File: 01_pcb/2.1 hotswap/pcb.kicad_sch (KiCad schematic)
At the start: 138 parts, among them J1 TYPE-C-31-M12_13, J2 AVR-ISP-6_mod, J3 Conn_01x01, J4 Conn_01x01, J5 Conn_01x01, J6 Conn_01x01, J7 Conn_01x01, J8 4PIN, K1 KEYSW, K10 KEYSW, K11 KEYSW, K12 KEYSW, K13 KEYSW, K14 KEYSW, K15 KEYSW, K16 KEYSW, K17 KEYSW, K18 KEYSW, K19 KEYSW, K2 KEYSW, K20 KEYSW, K21 KEYSW, K22 KEYSW, K23 KEYSW, K24 KEYSW, K25 KEYSW, K26 KEYSW, K27 KEYSW, K28 KEYSW, K29 KEYSW, K3 KEYSW, K30 KEYSW, K31 KEYSW, K32 KEYSW, K33 KEYSW, K34 KEYSW, K35 KEYSW, K36 KEYSW, K37 KEYSW, K38 KEYSW, K39 KEYSW, K4 KEYSW, K40 KEYSW, K41 KEYSW, K42 KEYSW, K43 KEYSW, K44 KEYSW, K45 KEYSW, K46 KEYSW, K47 KEYSW, K48 KEYSW, K49 KEYSW, K5 KEYSW, K50 KEYSW, K51 KEYSW, K52 KEYSW, K6 KEYSW, K7 KEYSW, K8 KEYSW, K9 KEYSW, SW1 SW_PUSH, SW2 Rotary_Encoder_Switch, U1 ATMEGA32U4, U2 PRTR5V0U2X, Y1 16MHz

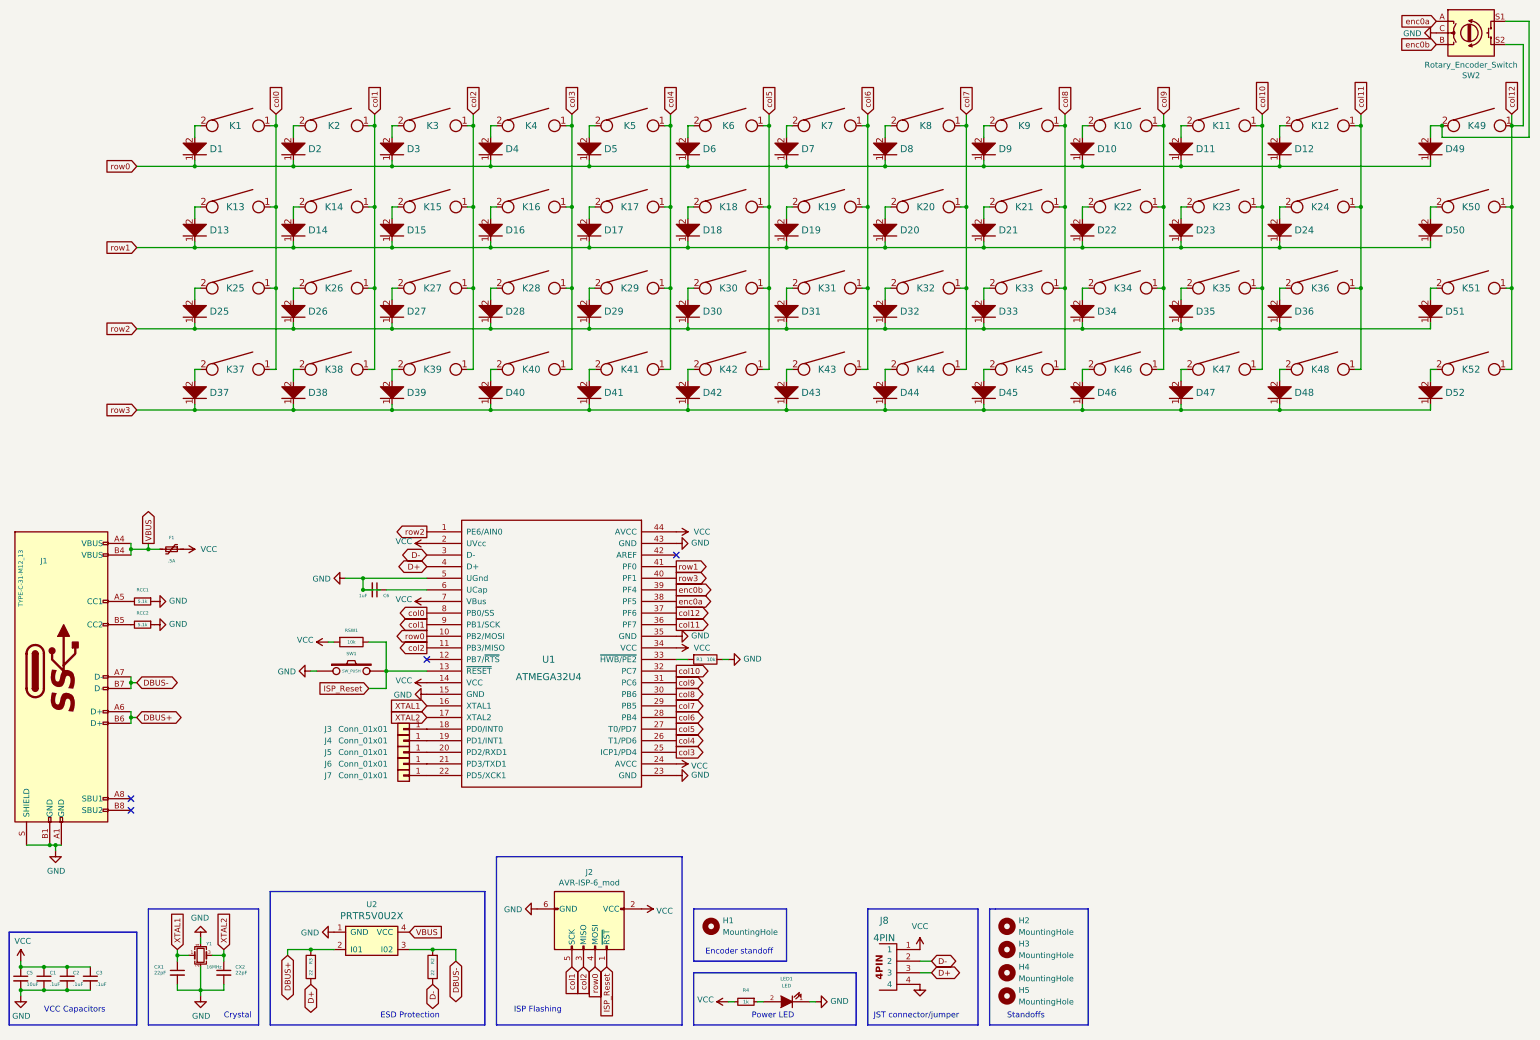
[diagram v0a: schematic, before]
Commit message: remove flex cuts and encoder
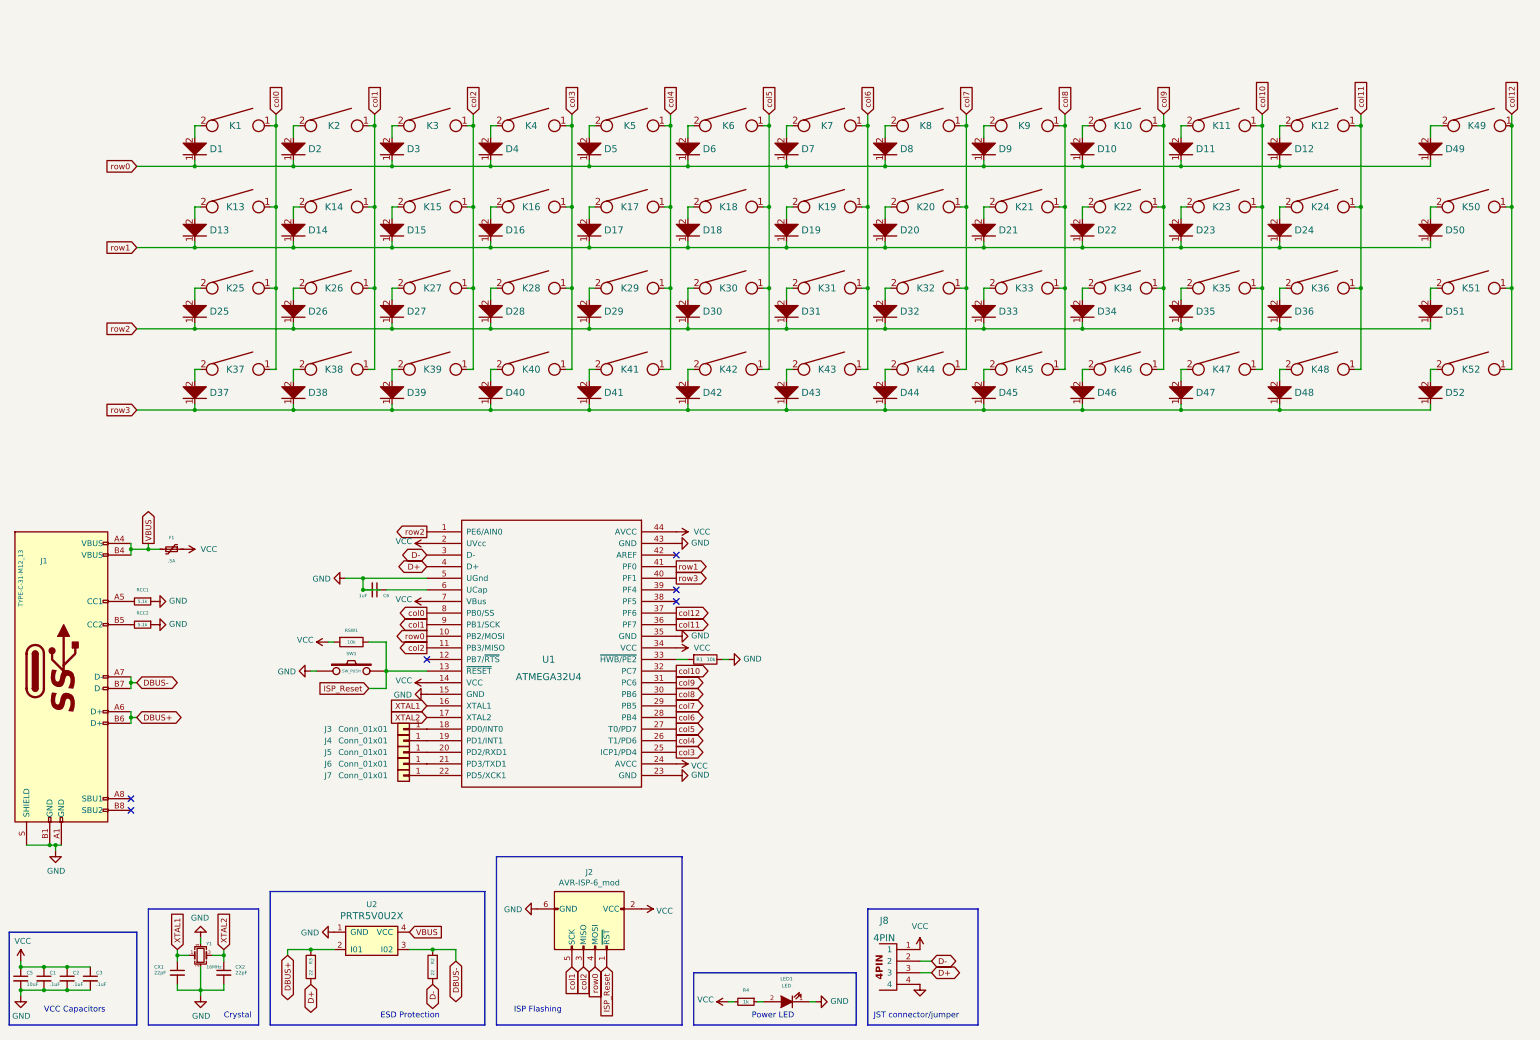
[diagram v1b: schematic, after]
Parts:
- removed H1, H2, H3, H4, H5: MountingHole, MountingHole:MountingHole_2.2mm_M2_DIN965_Pad, symbol Mechanical:MountingHole
- removed SW2: Rotary_Encoder_Switch, Keebio-Parts:RotaryEncoder_EC11, symbol Device:Rotary_Encoder_Switch
- K49: footprint MX_Only:MXOnly-1U-NoLED -> MX_Only:MXOnly-1U-Hotswap
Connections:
- net enc0a: no longer names the net of U1.38 (PF5)
- net enc0b: no longer names the net of U1.39 (PF4)
- no-connect marks 4 -> 6
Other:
- note removed: "Encoder standoff"
- note removed: "Standoffs"

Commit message: add 3d models to kicad footprints
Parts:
- R1, R2, R3, R4, RCC1, RCC2, RSW1: footprint Resistor_SMD:R_0805_2012Metric_Pad1.15x1.40mm_HandSolder -> Keeb_footprints:R_0805_2012Metric_Pad1.20x1.40mm_HandSolder
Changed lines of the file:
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@@
       (effects (font (size 0.7112 0.7112)))
     )
-    (property "Footprint" "Resistor_SMD:R_0805_2012Metric_Pad1.15x1.40mm_HandSolder" (id 2) (at 72.39 154.94 0)
+    (property "Footprint" "Keeb_footprints:R_0805_2012Metric_Pad1.20x1.40mm_HandSolder" (id 2) (at 72.39 154.94 0)
       (effects (font (size 1.27 1.27)) hide)
     )
@@
       (effects (font (size 0.7112 0.7112)))
     )
-    (property "Footprint" "Resistor_SMD:R_0805_2012Metric_Pad1.15x1.40mm_HandSolder" (id 2) (at 72.39 149.86 0)
+    (property "Footprint" "Keeb_footprints:R_0805_2012Metric_Pad1.20x1.40mm_HandSolder" (id 2) (at 72.39 149.86 0)
       (effects (font (size 1.27 1.27)) hide)
     )
@@
       (effects (font (size 0.7112 0.7112)))
     )
-    (property "Footprint" "Resistor_SMD:R_0805_2012Metric_Pad1.15x1.40mm_HandSolder" (id 2) (at 118.11 156.972 90)
+    (property "Footprint" "Keeb_footprints:R_0805_2012Metric_Pad1.20x1.40mm_HandSolder" (id 2) (at 118.11 156.972 90)
       (effects (font (size 1.27 1.27)) hide)
     )
@@
       (effects (font (size 0.762 0.762)))
     )
-    (property "Footprint" "Resistor_SMD:R_0805_2012Metric_Pad1.15x1.40mm_HandSolder" (id 2) (at 195.58 160.782 90)
+    (property "Footprint" "Keeb_footprints:R_0805_2012Metric_Pad1.20x1.40mm_HandSolder" (id 2) (at 195.58 160.782 90)
       (effects (font (size 1.27 1.27)) hide)
     )
@@
       (effects (font (size 0.7112 0.7112)))
     )
-    (property "Footprint" "Resistor_SMD:R_0805_2012Metric_Pad1.15x1.40mm_HandSolder" (id 2) (at 137.668 229.87 90)
+    (property "Footprint" "Keeb_footprints:R_0805_2012Metric_Pad1.20x1.40mm_HandSolder" (id 2) (at 137.668 229.87 90)
       (effects (font (size 1.27 1.27)) hide)
     )
@@
       (effects (font (size 0.7112 0.7112)))
     )
-    (property "Footprint" "Resistor_SMD:R_0805_2012Metric_Pad1.15x1.40mm_HandSolder" (id 2) (at 110.998 229.87 90)
+    (property "Footprint" "Keeb_footprints:R_0805_2012Metric_Pad1.20x1.40mm_HandSolder" (id 2) (at 110.998 229.87 90)
       (effects (font (size 1.27 1.27)) hide)
     )
@@
       (effects (font (size 0.762 0.762)))
     )
-    (property "Footprint" "Resistor_SMD:R_0805_2012Metric_Pad1.15x1.40mm_HandSolder" (id 2) (at 204.47 237.49 0)
+    (property "Footprint" "Keeb_footprints:R_0805_2012Metric_Pad1.20x1.40mm_HandSolder" (id 2) (at 204.47 237.49 0)
       (effects (font (size 1.27 1.27)) hide)
     )
@@
     )
     (path "/00000000-0000-0000-0000-00005e28a0b7"
-      (reference "R1") (unit 1) (value "10k") (footprint "Resistor_SMD:R_0805_2012Metric_Pad1.15x1.40mm_HandSolder")
+      (reference "R1") (unit 1) (value "10k") (footprint "Keeb_footprints:R_0805_2012Metric_Pad1.20x1.40mm_HandSolder")
     )
     (path "/00000000-0000-0000-0000-00005e4290ae"
-      (reference "R2") (unit 1) (value "22") (footprint "Resistor_SMD:R_0805_2012Metric_Pad1.15x1.40mm_HandSolder")
+      (reference "R2") (unit 1) (value "22") (footprint "Keeb_footprints:R_0805_2012Metric_Pad1.20x1.40mm_HandSolder")
     )
     (path "/00000000-0000-0000-0000-00005e44c75b"
-      (reference "R3") (unit 1) (value "22") (footprint "Resistor_SMD:R_0805_2012Metric_Pad1.15x1.40mm_HandSolder")
+      (reference "R3") (unit 1) (value "22") (footprint "Keeb_footprints:R_0805_2012Metric_Pad1.20x1.40mm_HandSolder")
     )
     (path "/00000000-0000-0000-0000-00005f9dc91d"
-      (reference "R4") (unit 1) (value "1k") (footprint "Resistor_SMD:R_0805_2012Metric_Pad1.15x1.40mm_HandSolder")
+      (reference "R4") (unit 1) (value "1k") (footprint "Keeb_footprints:R_0805_2012Metric_Pad1.20x1.40mm_HandSolder")
     )
     (path "/00000000-0000-0000-0000-00005dd97927"
-      (reference "RCC1") (unit 1) (value "5.1k") (footprint "Resistor_SMD:R_0805_2012Metric_Pad1.15x1.40mm_HandSolder")
+      (reference "RCC1") (unit 1) (value "5.1k") (footprint "Keeb_footprints:R_0805_2012Metric_Pad1.20x1.40mm_HandSolder")
     )
     (path "/00000000-0000-0000-0000-00005dd95fdc"
-      (reference "RCC2") (unit 1) (value "5.1k") (footprint "Resistor_SMD:R_0805_2012Metric_Pad1.15x1.40mm_HandSolder")
+      (reference "RCC2") (unit 1) (value "5.1k") (footprint "Keeb_footprints:R_0805_2012Metric_Pad1.20x1.40mm_HandSolder")
     )
     (path "/00000000-0000-0000-0000-00005e1f1159"
-      (reference "RSW1") (unit 1) (value "10k") (footprint "Resistor_SMD:R_0805_2012Metric_Pad1.15x1.40mm_HandSolder")
+      (reference "RSW1") (unit 1) (value "10k") (footprint "Keeb_footprints:R_0805_2012Metric_Pad1.20x1.40mm_HandSolder")
     )
     (path "/00000000-0000-0000-0000-00005e1efd9f"

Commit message: ¯\_(ツ)_/¯
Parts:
- removed J3, J4, J5, J6, J7: Conn_01x01, TestPoint:TestPoint_Keystone_5000-5004_Miniature, symbol Connector_Generic:Conn_01x01
- added J3: Conn_01x05_Female, Connector_PinHeader_2.54mm:PinHeader_1x05_P2.54mm_Vertical, symbol Connector:Conn_01x05_Female
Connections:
- net at U1.18 (PD0/INT0): now also J3.5 (Pin_5)
- net at U1.19 (PD1/INT1): now also J3.4 (Pin_4)
- net at U1.20 (PD2/RXD1): now also J3.3 (Pin_3)
- net at U1.21 (PD3/TXD1): now also J3.2 (Pin_2)
- net at U1.22 (PD5/XCK1): now also J3.1 (Pin_1)
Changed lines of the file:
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@@
     (pin "4")
   )
-  (symbol (lib_id "Connector_Generic:Conn_01x01") (at 129.54 177.8 180) (unit 1)
+  (symbol (lib_id "Connector:Conn_01x05_Female") (at 129.54 182.88 180) (unit 1)
     (in_bom yes) (on_board yes)
-    (property "Reference" "J3" (id 0) (at 113.03 177.8 0))
-    (property "Value" "Conn_01x01" (id 1) (at 120.65 177.8 0))
-    (property "Footprint" "TestPoint:TestPoint_Keystone_5000-5004_Miniature" (id 2) (at 129.54 177.8 0)
-      (effects (font (size 1.27 1.27)) hide)
-    )
-    (property "Datasheet" "~" (id 3) (at 129.54 177.8 0)
-      (effects (font (size 1.27 1.27)) hide)
-    )
-    (pin "1")
-  )
-  (symbol (lib_id "Connector_Generic:Conn_01x01") (at 129.54 187.96 180) (unit 1)
-    (in_bom yes) (on_board yes)
-    (property "Reference" "J7" (id 0) (at 113.03 187.96 0))
-    (property "Value" "Conn_01x01" (id 1) (at 120.65 187.96 0))
-    (property "Footprint" "TestPoint:TestPoint_Keystone_5000-5004_Miniature" (id 2) (at 129.54 187.96 0)
-      (effects (font (size 1.27 1.27)) hide)
-    )
-    (property "Datasheet" "~" (id 3) (at 129.54 187.96 0)
-      (effects (font (size 1.27 1.27)) hide)
-    )
-    (pin "1")
+    (property "Reference" "J3" (id 0) (at 130.175 172.72 0))
+    (property "Value" "Conn_01x05_Female" (id 1) (at 123.19 182.88 90))
+    (property "Footprint" "Connector_PinHeader_2.54mm:PinHeader_1x05_P2.54mm_Vertical" (id 2) (at 129.54 182.88 0)
+      (effects (font (size 1.27 1.27)) hide)
+    )
+    (property "Datasheet" "~" (id 3) (at 129.54 182.88 0)
+      (effects (font (size 1.27 1.27)) hide)
+    )
+    (pin "1")
+    (pin "2")
+    (pin "3")
+    (pin "4")
+    (pin "5")
   )
   (symbol (lib_id "power:VCC") (at 242.57 226.06 0) (unit 1)
@@
     )
     (property "Datasheet" "" (id 3) (at 242.57 226.06 0)
-      (effects (font (size 1.27 1.27)) hide)
-    )
-    (pin "1")
-  )
-  (symbol (lib_id "Connector_Generic:Conn_01x01") (at 129.54 182.88 180) (unit 1)
-    (in_bom yes) (on_board yes)
-    (property "Reference" "J5" (id 0) (at 113.03 182.88 0))
-    (property "Value" "Conn_01x01" (id 1) (at 120.65 182.88 0))
-    (property "Footprint" "TestPoint:TestPoint_Keystone_5000-5004_Miniature" (id 2) (at 129.54 182.88 0)
-      (effects (font (size 1.27 1.27)) hide)
-    )
-    (property "Datasheet" "~" (id 3) (at 129.54 182.88 0)
       (effects (font (size 1.27 1.27)) hide)
     )
@@
     (pin "4")
   )
-  (symbol (lib_id "Connector_Generic:Conn_01x01") (at 129.54 185.42 180) (unit 1)
-    (in_bom yes) (on_board yes)
-    (property "Reference" "J6" (id 0) (at 113.03 185.42 0))
-    (property "Value" "Conn_01x01" (id 1) (at 120.65 185.42 0))
-    (property "Footprint" "TestPoint:TestPoint_Keystone_5000-5004_Miniature" (id 2) (at 129.54 185.42 0)
-      (effects (font (size 1.27 1.27)) hide)
-    )
-    (property "Datasheet" "~" (id 3) (at 129.54 185.42 0)
-      (effects (font (size 1.27 1.27)) hide)
-    )
-    (pin "1")
-  )
-  (symbol (lib_id "Connector_Generic:Conn_01x01") (at 129.54 180.34 180) (unit 1)
-    (in_bom yes) (on_board yes)
-    (property "Reference" "J4" (id 0) (at 113.03 180.34 0))
-    (property "Value" "Conn_01x01" (id 1) (at 120.65 180.34 0))
-    (property "Footprint" "TestPoint:TestPoint_Keystone_5000-5004_Miniature" (id 2) (at 129.54 180.34 0)
-      (effects (font (size 1.27 1.27)) hide)
-    )
-    (property "Datasheet" "~" (id 3) (at 129.54 180.34 0)
-      (effects (font (size 1.27 1.27)) hide)
-    )
-    (pin "1")
-  )
   (symbol (lib_id "component:GND") (at 242.57 234.95 0) (unit 1)
     (in_bom yes) (on_board yes) (fields_autoplaced)
@@
       (reference "J2") (unit 1) (value "AVR-ISP-6_mod") (footprint "Keeb_footprints:ICSP-Header_small_pins")
     )
-    (path "/04d1ab82-ed8f-4d7d-a110-65a8711ffe2e"
-      (reference "J3") (unit 1) (value "Conn_01x01") (footprint "TestPoint:TestPoint_Keystone_5000-5004_Miniature")
-    )
-    (path "/7fd804ca-b198-4c51-a284-2540760b3701"
-      (reference "J4") (unit 1) (value "Conn_01x01") (footprint "TestPoint:TestPoint_Keystone_5000-5004_Miniature")
-    )
-    (path "/4b03cbe3-dede-4b6f-bdbc-e6a6e20ebbf4"
-      (reference "J5") (unit 1) (value "Conn_01x01") (footprint "TestPoint:TestPoint_Keystone_5000-5004_Miniature")
-    )
-    (path "/7609a3fa-d1d7-462f-b5ad-187c83525aa0"
-      (reference "J6") (unit 1) (value "Conn_01x01") (footprint "TestPoint:TestPoint_Keystone_5000-5004_Miniature")
-    )
-    (path "/1e98888a-427d-4a31-a7dd-97b8504ac365"
-      (reference "J7") (unit 1) (value "Conn_01x01") (footprint "TestPoint:TestPoint_Keystone_5000-5004_Miniature")
+    (path "/19d2ef2e-3dec-4d6d-ae1f-30bffe5a8b2f"
+      (reference "J3") (unit 1) (value "Conn_01x05_Female") (footprint "Connector_PinHeader_2.54mm:PinHeader_1x05_P2.54mm_Vertical")
     )
     (path "/4bae80ae-0865-4c99-8f93-5b3aff8a59f8"
